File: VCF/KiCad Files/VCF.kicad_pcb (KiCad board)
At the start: 2 copper layers, 145.9 x 128.5 mm, 79 parts, among them J1 AUDIO_IN, J2 CV1, J3 CV2, J4 AUDIO_OUT, J5 Conn_02x05_Odd_Even, J6 Conn_01x05_Male, J7 Conn_01x05_Female, J8 Conn_01x08_Male, J9 Conn_01x08_Female, SW1 SW_DPDT_x2, U1 TL074, U2 TL074

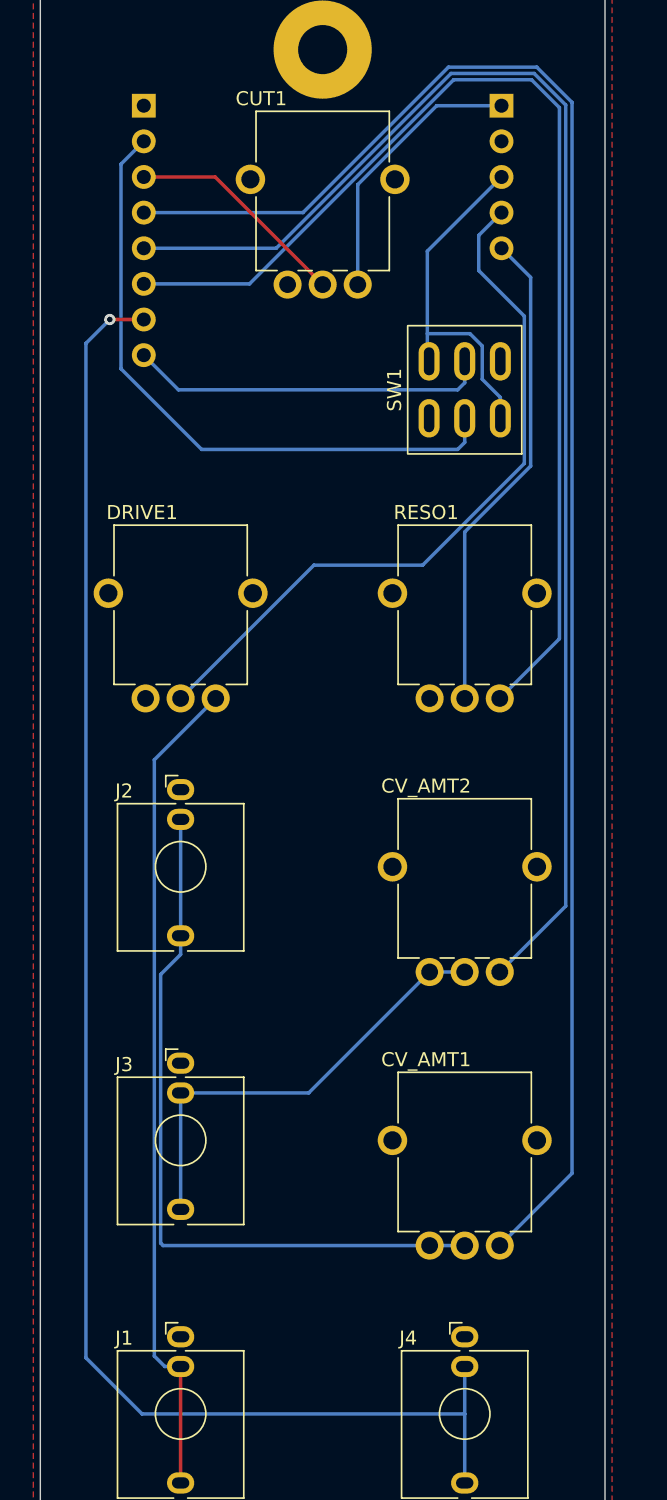
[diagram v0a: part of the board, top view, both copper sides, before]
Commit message: Corrected PCB
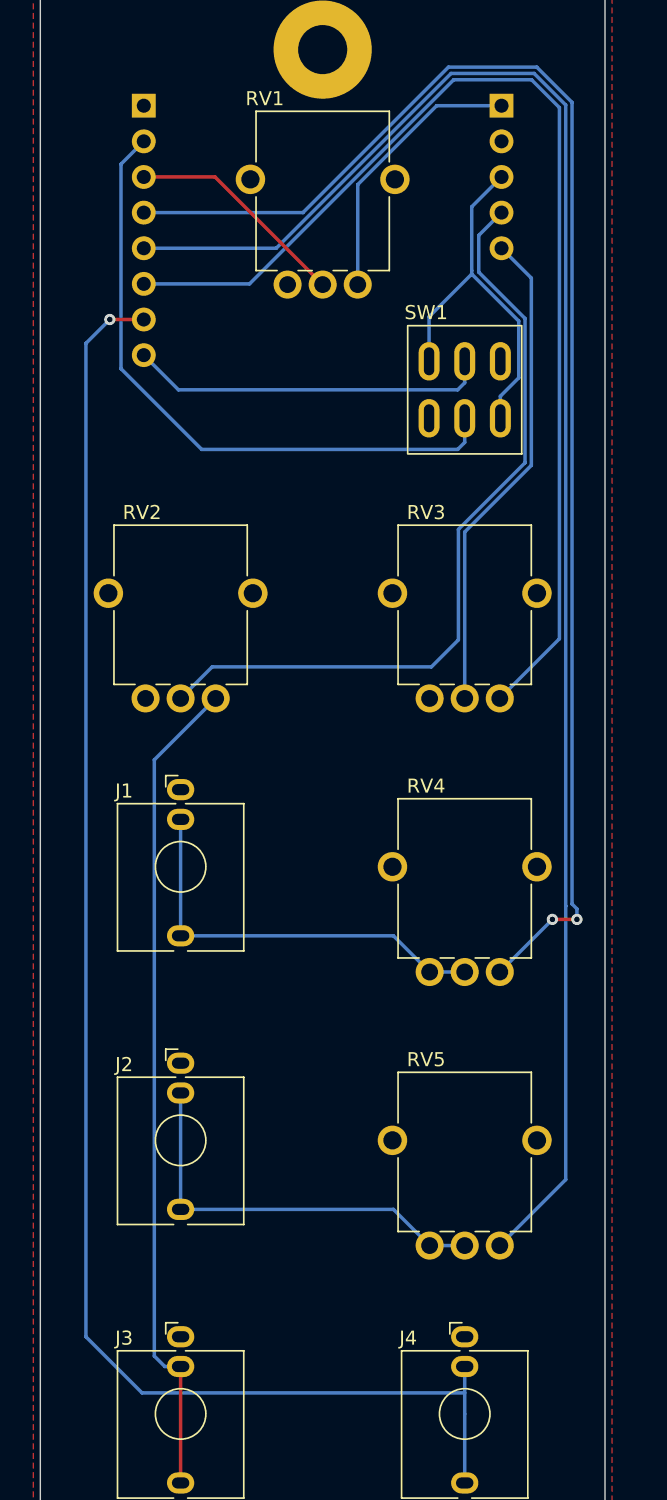
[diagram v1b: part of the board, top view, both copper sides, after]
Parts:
- moved RV4 19.5 mm to (130.2, 103.5)
- moved RV5 19.5 mm to (130.2, 123.0)
- renumbered J2 to J1, J3 to J2, J1 to J3, CUT1 to RV1, DRIVE1 to RV2, RESO1 to RV3, CV_AMT1 to RV4, CV_AMT2 to RV5
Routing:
- net Net-(RV4-Pad1): track 52.5 -> 29.6 mm
- net CV_AMT2_A: track 99.9 -> 119.4 mm
- net CV_AMT1_A: track 119.5 -> 101.3 mm, vias 0 -> 2
- net DRIVE1_A: track 51.3 -> 56.0 mm
- net Net-(RV5-Pad1): track 32.1 -> 29.6 mm
- net SW1A_IN_A: track 25.8 -> 27.5 mm
- net AUDIO_OUT_A: track 114.1 -> 112.6 mm

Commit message: Added gerber files
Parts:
- moved Ref** 0.28 mm to (73.8, 156.2)
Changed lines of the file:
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@@
       (drillshape 0)
       (scaleselection 1)
-      (outputdirectory "../Gerber Files/Panel/")
+      (outputdirectory "../Gerber Files/")
     )
   )
@@
   )
   (footprint "1_CUSTOM:logo_drachma_full_final_for_PCB" (layer "F.Cu")
-    (at 73.875 156.5)
+    (at 73.75 156.25)
     (attr through_hole)
     (fp_text reference "Ref**" (at 0 0) (layer "F.SilkS") hide

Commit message: Cleaned up schematic
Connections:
- net CUT1_A renamed CUTOFF_A
- net CUT1_B renamed CUTOFF_B
- net CV_AMT1_A renamed CV1_LVL_A
- net CV_AMT1_B renamed CV1_LVL_B
- net CV_AMT2_A renamed CV2_LVL_A
- net CV_AMT2_B renamed CV2_LVL_B
- net DRIVE1_A renamed DRIVE_A
- net DRIVE1_B renamed DRIVE_B
- net RESO1_IN_A renamed RES_IN_A
- net RESO1_IN_B renamed RES_IN_B
- net RESO1_OUT_A renamed RES_OUT_A
- net RESO1_OUT_B renamed RES_OUT_B

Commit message: Added PDF schematic
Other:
- board text added: "-12V"
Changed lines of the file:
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@@
     (property "Sheetname" "")
     (attr smd)
-    (fp_text reference "C6" (at -0.75 1.75 180) (layer "B.SilkS")
+    (fp_text reference "C6" (at 0 -2.03125 180) (layer "B.SilkS")
       (effects (font (size 1 1) (thickness 0.15)) (justify mirror))
     )
@@
     (property "Sheetname" "")
     (attr through_hole)
-    (fp_text reference "J5" (at 5.025 0.675) (layer "B.SilkS")
+    (fp_text reference "J5" (at 1.27 2.925) (layer "B.SilkS")
       (effects (font (size 1 1) (thickness 0.15)) (justify mirror))
     )
@@
     (property "Sheetname" "")
     (attr smd)
-    (fp_text reference "D13" (at -4.5 -1.75 90) (layer "B.SilkS")
+    (fp_text reference "D13" (at 0 -1.75 90) (layer "B.SilkS")
       (effects (font (size 1 1) (thickness 0.15)) (justify mirror))
     )
@@
     (property "Sheetname" "")
     (attr smd)
-    (fp_text reference "D14" (at 4.5 -1.75 90) (layer "B.SilkS")
+    (fp_text reference "D14" (at 0 -1.75 90) (layer "B.SilkS")
       (effects (font (size 1 1) (thickness 0.15)) (justify mirror))
     )
@@
     )
   )
+  (gr_line (start 167 51.655) (end 167 57) (layer "B.SilkS") (width 0.25))
   (gr_line (start 53.375 103.5) (end 73.625 103.5) (layer "F.SilkS") (width 0.25))
   (gr_line (start 43.375 37) (end 83.625 37) (layer "F.SilkS") (width 0.25))
@@
   (gr_rect (start 100 40) (end 140.25 150) (layer "Edge.Cuts") (width 0.1) (fill none))
   (gr_rect (start 43.375 30.75) (end 83.625 159.25) (layer "Edge.Cuts") (width 0.1) (fill none))
+  (gr_text "-12V" (at 165.75 54.75 270) (layer "B.SilkS")
+    (effects (font (size 1 1) (thickness 0.15)) (justify mirror))
+  )
   (gr_text "MORITZ KLEIN" (at 77.625 32.5) (layer "F.SilkS")
     (effects (font (size 1 1) (thickness 0.2)))

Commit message: Added BOM
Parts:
- C1, C7: footprint Capacitor_SMD:C_0603_1608Metric_Pad1.08x0.95mm_HandSolder -> Capacitor_SMD:C_1206_3216Metric_Pad1.33x1.80mm_HandSolder
- C10, C11, C8, C9: footprint Capacitor_SMD:C_0603_1608Metric_Pad1.08x0.95mm_HandSolder -> Capacitor_SMD:C_0805_2012Metric_Pad1.18x1.45mm_HandSolder
- R1, R10, R11, R12, R13, R14, R15, R16, R17, R18, R19, R2, R20, R22, R23, R3, R4, R5, R6, R7, R8, R9: footprint Resistor_SMD:R_0603_1608Metric_Pad0.98x0.95mm_HandSolder -> Resistor_SMD:R_0805_2012Metric_Pad1.20x1.40mm_HandSolder
- moved R20 4.01 mm to (168.0, 91.8), turned to 0 degrees
- moved C3 3.75 mm to (176.8, 92.0)
- moved C4 3.75 mm to (174.2, 100.5)
- moved C5 3.75 mm to (171.8, 92.0)
- moved D1 3.75 mm to (180.5, 96.2)
- moved D2 3.75 mm to (178.0, 96.2)
- moved D3 3.75 mm to (175.5, 96.2)
- moved D4 3.75 mm to (173.0, 96.2)
- moved D5 3.75 mm to (170.5, 96.2)
- moved D6 3.75 mm to (168.0, 96.2)
- moved C2 3.75 mm to (179.3, 100.5)
- moved C6 3.75 mm to (169.3, 100.5)
- moved C7 3.59 mm to (167.5, 89.2)
- moved R19 3.01 mm to (168.0, 86.8)
- moved R18 3.01 mm to (180.5, 86.8)
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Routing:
- net SW1B_OUT_B: track 36.4 -> 48.8 mm
- net Net-(D6-Pad1): track 45.7 -> 51.4 mm
- net AUDIO_OUT_B: track 26.4 -> 31.6 mm
- net Net-(D13-Pad2): track 16.7 -> 21.9 mm, vias 2 -> 4
- net SW1A_OUT_B: track 55.0 -> 59.7 mm
- net Net-(D16-Pad1): track 39.9 -> 44.4 mm
- net Net-(D1-Pad2): track 18.9 -> 22.9 mm
- net RES_OUT_B: track 30.3 -> 33.9 mm
- net RES_IN_B: track 35.8 -> 38.4 mm
- net +12V: track 69.6 -> 72.1 mm
- net -12V: track 44.7 -> 47.2 mm
- net DRIVE_B: track 8.98 -> 11.4 mm
- net CV2_LVL_B: track 16.8 -> 18.8 mm
- net SW1A_IN_B: track 17.0 -> 18.9 mm
- net CV1_LVL_B: track 17.5 -> 19.1 mm
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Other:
- outline, holes or cut-outs redrawn

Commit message: Updated panel
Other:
- board text added: "+"
- board text added: "-"
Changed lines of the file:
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@@
   )
   (gr_line (start 167 50.905) (end 167 56.25) (layer "B.SilkS") (width 0.25))
-  (gr_line (start 53.375 103.5) (end 73.625 103.5) (layer "F.SilkS") (width 0.25))
+  (gr_line (start 53.375 103.5) (end 65.375 103.5) (layer "F.SilkS") (width 0.25))
+  (gr_circle (center 73.625 123) (end 81.875 123) (layer "F.SilkS") (width 0.25) (fill none))
+  (gr_circle (center 73.625 84) (end 81.875 84) (layer "F.SilkS") (width 0.25) (fill none))
+  (gr_circle (center 53.375 84) (end 61.625 84) (layer "F.SilkS") (width 0.25) (fill none))
   (gr_line (start 43.375 37) (end 83.625 37) (layer "F.SilkS") (width 0.25))
+  (gr_circle (center 63.5 54.5) (end 74.5 54.5) (layer "F.SilkS") (width 0.25) (fill none))
   (gr_line (start 43.375 153) (end 83.625 153) (layer "F.SilkS") (width 0.25))
-  (gr_line (start 53.375 123) (end 73.625 123) (layer "F.SilkS") (width 0.25))
+  (gr_line (start 53.375 123) (end 65.375 123) (layer "F.SilkS") (width 0.25))
+  (gr_line (start 53.375 75.75) (end 53.375 73.375) (layer "F.SilkS") (width 0.25))
+  (gr_circle (center 73.625 103.5) (end 81.875 103.5) (layer "F.SilkS") (width 0.25) (fill none))
+  (gr_circle (center 73.625 69.5) (end 78.125 69.5) (layer "F.SilkS") (width 0.25) (fill none))
   (gr_circle (center 130.25 103.5) (end 137.75 103.5) (layer "Dwgs.User") (width 0.1) (fill none))
   (gr_circle (center 130.25 123) (end 137.75 123) (layer "Dwgs.User") (width 0.1) (fill none))
@@
     (effects (font (size 1.5 1.5) (thickness 0.25)))
   )
-  (gr_text "LVL" (at 73.625 113.5) (layer "F.SilkS")
+  (gr_text "LVL" (at 73.625 113.375) (layer "F.SilkS")
     (effects (font (size 1.5 1.5) (thickness 0.25)))
   )
@@
     (effects (font (size 1.5 1.5) (thickness 0.25)))
   )
+  (gr_text "-" (at 51.25 74.25) (layer "F.SilkS")
+    (effects (font (size 1.5 1.5) (thickness 0.15)))
+  )
   (gr_text "BP" (at 80.125 69.5) (layer "F.SilkS")
     (effects (font (size 1.5 1.5) (thickness 0.25)))
   )
-  (gr_text "DRIVE" (at 53.375 94) (layer "F.SilkS")
-    (effects (font (size 1.5 1.5) (thickness 0.25)))
-  )
-  (gr_text "LVL" (at 73.625 133) (layer "F.SilkS")
+  (gr_text "+" (at 55.5 74.25) (layer "F.SilkS")
+    (effects (font (size 1.5 1.5) (thickness 0.15)))
+  )
+  (gr_text "DRIVE" (at 53.375 93.875) (layer "F.SilkS")
+    (effects (font (size 1.5 1.5) (thickness 0.25)))
+  )
+  (gr_text "LVL" (at 73.625 132.875) (layer "F.SilkS")
     (effects (font (size 1.5 1.5) (thickness 0.25)))
   )
@@
     (effects (font (size 1.5 1.5) (thickness 0.25)))
   )
-  (gr_text "RESONANCE" (at 73.625 94) (layer "F.SilkS")
+  (gr_text "RESONANCE" (at 73.625 93.875) (layer "F.SilkS")
     (effects (font (size 1.5 1.5) (thickness 0.25)))
   )
@@
   (dimension (type orthogonal) (layer "Dwgs.User")
     (pts (xy 53.375 84) (xy 43.375 84.25))
-    (height -8.25)
-    (orientation 0)
-    (gr_text "10.0000 mm" (at 48.375 74.6) (layer "Dwgs.User")
-      (effects (font (size 1 1) (thickness 0.15)))
-    )
+    (height -11.25)
+    (orientation 0)
+    (gr_text "10.0000 mm" (at 48.375 71.6) (layer "Dwgs.User")
+      (effects (font (size 1 1) (thickness 0.15)))
+    )

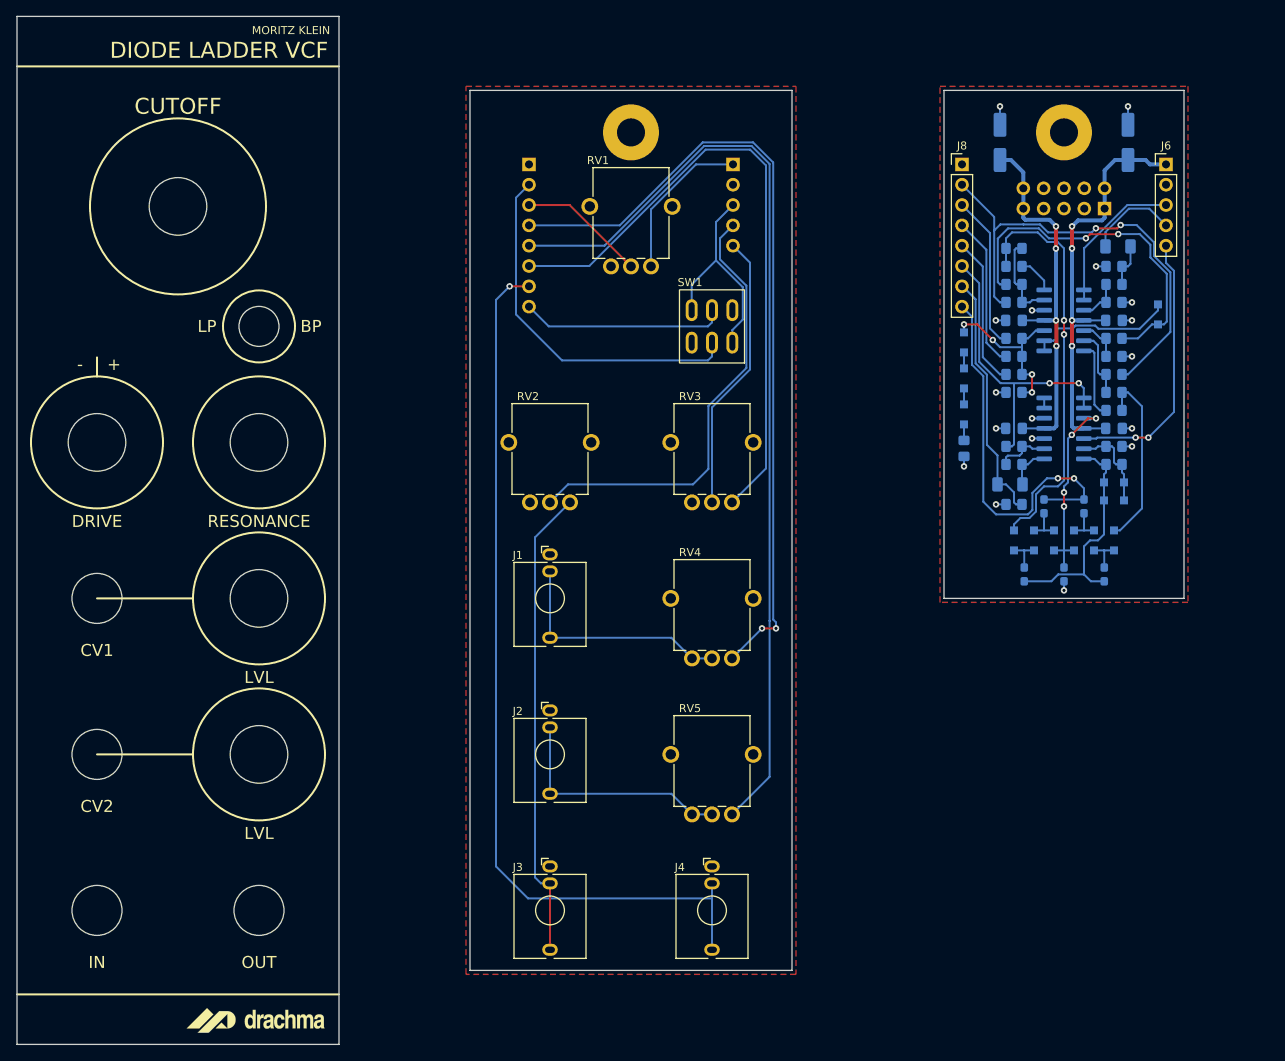
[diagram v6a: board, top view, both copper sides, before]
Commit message: Corrected footprints
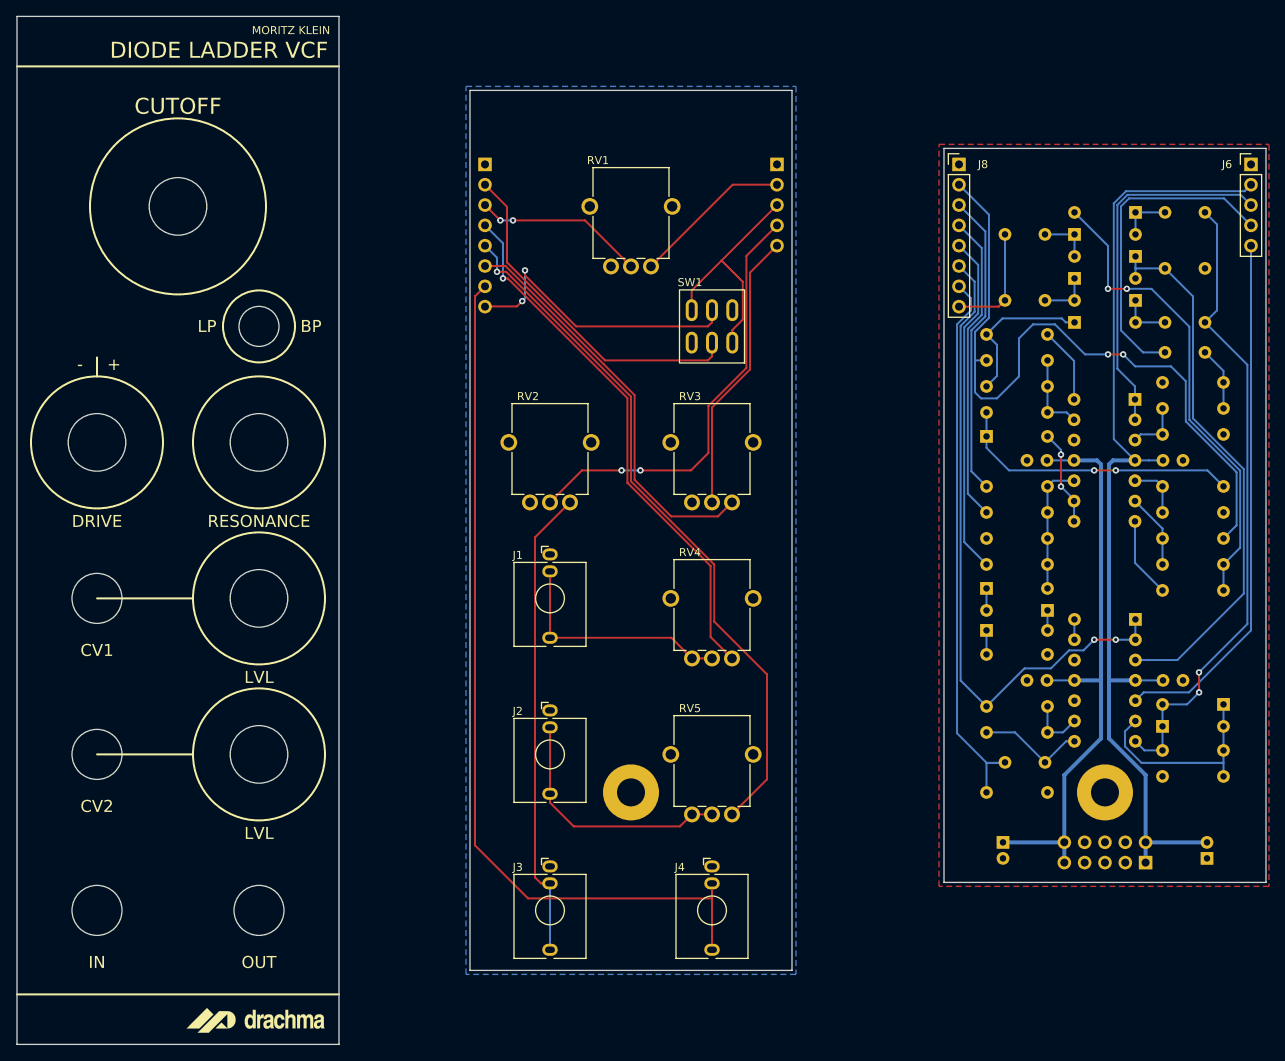
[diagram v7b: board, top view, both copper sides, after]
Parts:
- removed the REF** at (174.2, 45.2)
- added ?: , , F.Cu at (179.4, 127.8)
- C1, C7: footprint Capacitor_SMD:C_1206_3216Metric_Pad1.33x1.80mm_HandSolder -> Capacitor_THT:C_Rect_L7.2mm_W3.5mm_P5.00mm_FKS2_FKP2_MKS2_MKP2
- C10, C11, C8, C9: footprint Capacitor_SMD:C_0805_2012Metric_Pad1.18x1.45mm_HandSolder -> Capacitor_THT:C_Disc_D3.8mm_W2.6mm_P2.50mm
- C12, C13: footprint Capacitor_SMD:CP_Elec_5x5.4 -> Capacitor_THT:CP_Radial_D5.0mm_P2.00mm
- C2, C3, C4, C5, C6: footprint Capacitor_SMD:C_0603_1608Metric_Pad1.08x0.95mm_HandSolder -> Capacitor_THT:C_Rect_L7.2mm_W2.5mm_P5.00mm_FKS2_FKP2_MKS2_MKP2
- D1, D13, D14, D15, D16, D2, D3, D4, D5, D6, D7, D8: footprint Diode_SMD:D_SOD-323_HandSoldering -> Diode_THT:D_DO-35_SOD27_P7.62mm_Horizontal
- R1, R10, R11, R12, R13, R14, R15, R16, R17, R18, R19, R2, R20, R22, R23, R3, R4, R5, R6, R7, R8, R9: footprint Resistor_SMD:R_0805_2012Metric_Pad1.20x1.40mm_HandSolder -> Resistor_THT:R_Axial_DIN0207_L6.3mm_D2.5mm_P7.62mm_Horizontal
- U1, U2: footprint Package_SO:SOIC-14_3.9x8.7mm_P1.27mm -> Package_DIP:DIP-14_W7.62mm
- moved C12 90.0 mm to (192.1, 136.0), turned to 90 degrees
- moved C13 87.5 mm to (166.6, 134.0), turned to -90 degrees
- moved ? 82.5 mm to (120.1, 127.8)
- moved J5 81.9 mm to (184.4, 136.5)
- moved C2 47.0 mm to (191.9, 55.2), turned to 180 degrees
- moved C4 42.1 mm to (191.9, 62.2), turned to 180 degrees
- moved R16 41.7 mm to (186.6, 125.8), turned to 0 degrees
- moved D1 41.1 mm to (183.2, 55.2), turned to 180 degrees
- moved C6 38.8 mm to (191.9, 69.0), turned to 180 degrees
- moved D2 38.3 mm to (175.6, 58.0), turned to 0 degrees
- moved R18 38.3 mm to (194.2, 122.5)
- moved D3 36.3 mm to (183.2, 60.8), turned to 180 degrees
- moved R20 36.2 mm to (172.2, 127.8), turned to 180 degrees
- moved C3 35.4 mm to (166.9, 58.0), turned to 0 degrees
- moved C7 35.0 mm to (171.9, 124.0)
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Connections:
- J6 pad 1: +12V -> GND
- J6 pad 2: GND -> +12V
- J7 pad 1: +12V -> GND
- J7 pad 2: GND -> +12V
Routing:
- net +12V: track 72.1 -> 144.4 mm, vias 4 -> 0
- net RES_FB: track 29.3 -> 80.8 mm, vias 0 -> 2
- net RES_IN_B: track 38.4 -> 82.5 mm
- net Net-(C4-Pad2): track 24.9 -> 68.2 mm, vias 4 -> 0
- net Net-(D1-Pad2): track 22.9 -> 59.9 mm, vias 0 -> 2
- net AUDIO_OUT_B: track 31.6 -> 68.5 mm
- net SW1B_OUT_B: track 48.8 -> 14.3 mm, vias 2 -> 0
- net CV1_LVL_A: track 101.3 -> 67.3 mm, vias 2 -> 1
- net RES_OUT_B: track 33.9 -> 66.2 mm, vias 2 -> 0
- net Net-(D6-Pad1): track 51.4 -> 19.6 mm, vias 2 -> 0
- net CV2_LVL_A: track 119.4 -> 88.2 mm, vias 0 -> 1
- net RES_IN_A: track 80.3 -> 50.8 mm
- net SW1A_OUT_B: track 59.7 -> 88.9 mm
- net DRIVE_B: track 11.4 -> 40.2 mm
- net SW1A_IN_B: track 18.9 -> 45.5 mm
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- added copper zone on B.Cu, net GND
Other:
- board size 145.9 x 128.5 mm -> 156.1 x 128.5 mm
